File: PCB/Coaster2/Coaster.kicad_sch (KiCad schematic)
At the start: 277 parts, among them J1 Reset, J2 TC2030-USB-NL-DS, J3 USB-C-Socket-H, U1 ICS43434_MEMS_Mic, U2 ESP32-S3-MINI-1, U3 MD8942

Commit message: PCB Update
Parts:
- C131: JLCPCB Rotation Offset 180 -> (none); LCSC Part # C122649 -> (none); MPN (none) -> C122649
- C133, C135, C136, C137: LCSC Part # C194427 -> (none); MPN (none) -> C194427
- C138: LCSC Part # C1691 -> (none); MPN (none) -> C1691
- D1, D10, D100, D101, D102, D103, D104, D105, D106, D107, D108, D109, D11, D110, D111, D112, D113, D114, D115, D116, D117, D118, D119, D12, D120, D121, D122, D123, D124, D13, D14, D15, D16, D17, D18, D19, D2, D20, D21, D22, D23, D24, D25, D26, D27, D28, D29, D3, D30, D31, D32, D33, D34, D35, D36, D37, D38, D39, D4, D40, D41, D42, D43, D44, D45, D46, D47, D48, D49, D5, D50, D51, D52, D53, D54, D55, D56, D57, D58, D59, D6, D60, D61, D62, D63, D64, D65, D66, D67, D68, D69, D7, D70, D71, D72, D73, D74, D75, D76, D77, D78, D79, D8, D80, D81, D82, D83, D84, D85, D86, D87, D88, D89, D9, D90, D91, D92, D93, D94, D95, D96, D97, D98, D99: LCSC Part # C5349953 -> (none); MPN (none) -> C5349953
- J3: LCSC Part # C709357 -> (none); MPN (none) -> C709357
- U1: LCSC Part # C5656610 -> (none); MPN (none) -> C5656610
- U2: LCSC Part # C3013941 -> (none); MPN (none) -> C3013941
- U3: LCSC Part # C2684786 -> (none); MPN (none) -> C2684786; Rotation Offset 180 -> (none)

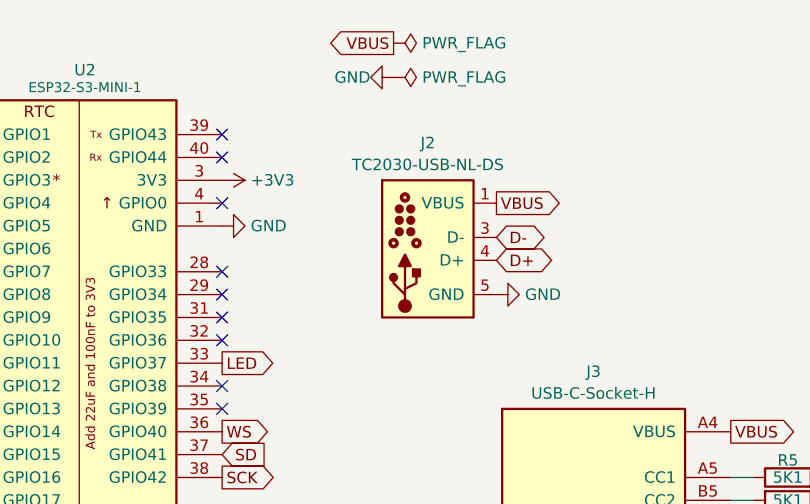
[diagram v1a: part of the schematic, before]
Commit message: Fixed render
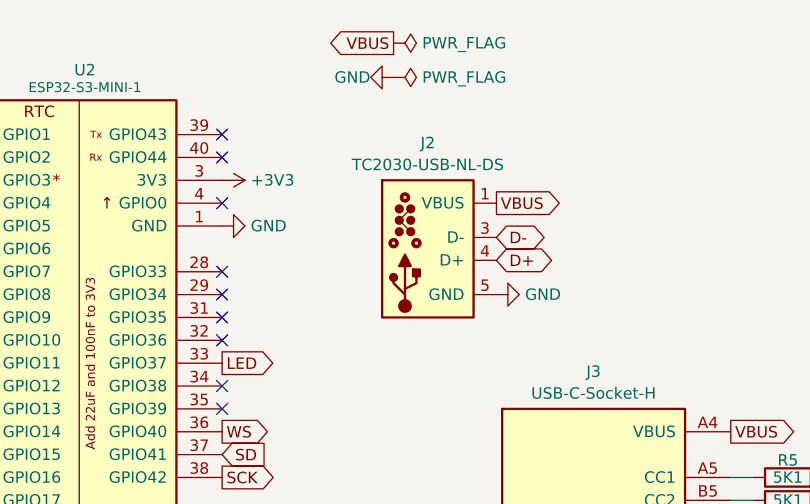
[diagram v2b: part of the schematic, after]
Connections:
- net D-: now also J2.2 (NC), J2.6 (NC)
- net GND: no longer J2.6 (GND)
- net VBUS: no longer J2.2 (VBUS)

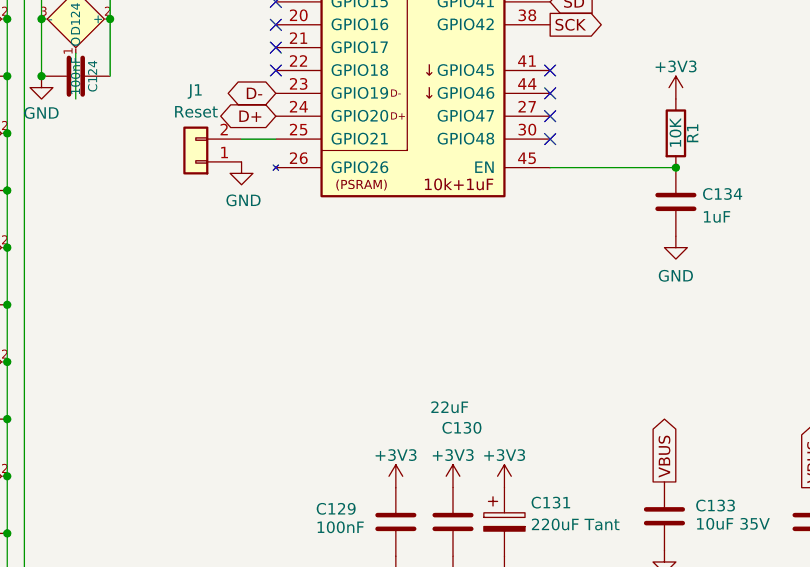
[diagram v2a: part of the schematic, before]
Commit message: WAGO power pads
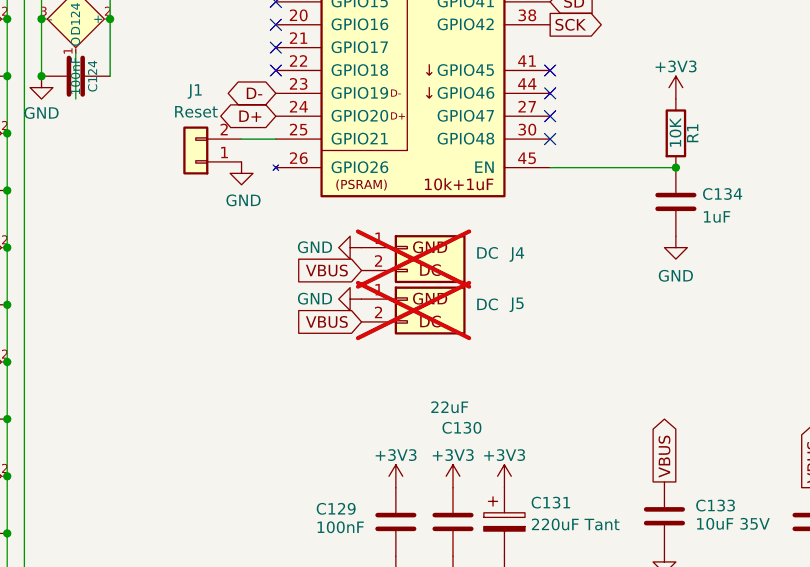
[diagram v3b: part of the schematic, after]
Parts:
- added J4, J5: DC, RevK:WAGO-2060-452-998-404, symbol RevK:PowerIn
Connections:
- net GND: now also J4.1 (GND), J5.1 (GND)
- net VBUS: now also J4.2 (DC), J5.2 (DC)
